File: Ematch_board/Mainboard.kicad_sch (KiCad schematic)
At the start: 69 parts, among them J10 Conn_01x02_Male, J11 Conn_Coaxial, J7 RBUS, J8 USB_C_Receptacle_USB2.0, J9 Conn_01x02_Male, Q1 MMDT2222A, U2 LTC4411, U3 SC4216H, U4 LTC4411, U5 SN65HVD230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

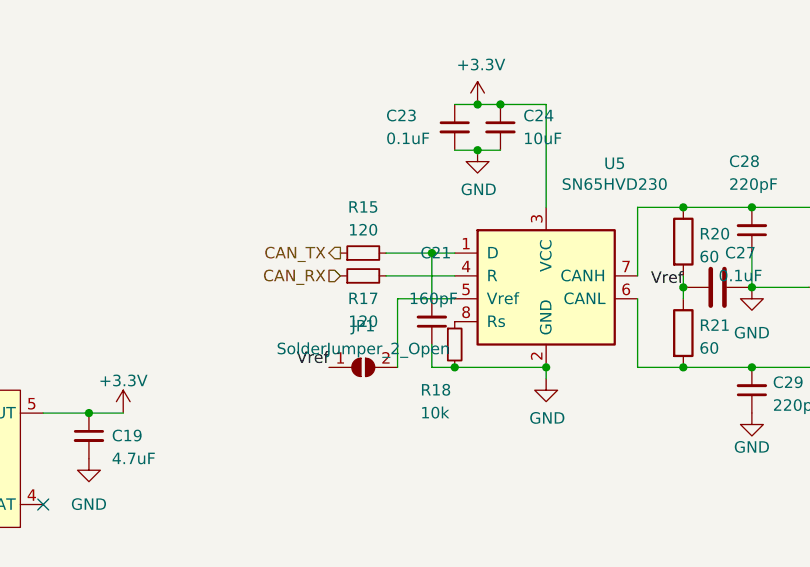
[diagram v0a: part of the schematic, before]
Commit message: Removed CAN resistors
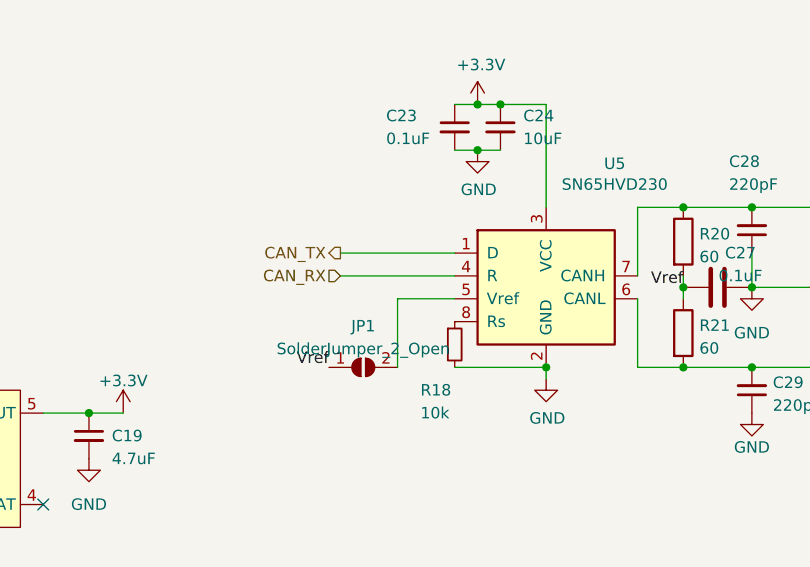
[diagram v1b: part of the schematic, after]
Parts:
- removed C21: 160pF, Capacitor_SMD:C_0603_1608Metric, symbol Device:C_Small
- removed R15, R17: 120, Resistor_SMD:R_0603_1608Metric, symbol Device:R_Small
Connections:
- net CAN_RX: now also U5.4 (R)
- net CAN_TX: now also U5.1 (D)
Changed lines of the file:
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@@
 (kicad_sch (version 20211123) (generator eeschema)
   (paper "A4")
-  (junction (at 190.5 162.56) (diameter 0) (color 0 0 0 0)
-  )
   (junction (at 219.71 53.34) (diameter 0) (color 0 0 0 0)
   )
@@
   (junction (at 203.2 106.68) (diameter 0) (color 0 0 0 0)
   )
-  (junction (at 187.96 149.86) (diameter 0) (color 0 0 0 0)
-  )
   (junction (at 199.39 38.1) (diameter 0) (color 0 0 0 0)
   )
@@
     (stroke (width 0) (type default) (color 0 0 0 0))
   )
-  (wire (pts (xy 187.96 160.02) (xy 187.96 162.56))
-    (stroke (width 0) (type default) (color 0 0 0 0))
-  )
   (wire (pts (xy 149.86 167.64) (xy 153.67 167.64))
     (stroke (width 0) (type default) (color 0 0 0 0))
@@
     (stroke (width 0) (type default) (color 0 0 0 0))
   )
-  (wire (pts (xy 182.88 152.4) (xy 190.5 152.4))
+  (wire (pts (xy 177.8 152.4) (xy 190.5 152.4))
     (stroke (width 0) (type default) (color 0 0 0 0))
   )
@@
     (stroke (width 0) (type default) (color 0 0 0 0))
   )
-  (wire (pts (xy 187.96 154.94) (xy 187.96 149.86))
-    (stroke (width 0) (type default) (color 0 0 0 0))
-  )
   (wire (pts (xy 124.46 93.98) (xy 132.08 93.98))
     (stroke (width 0) (type default) (color 0 0 0 0))
@@
     (stroke (width 0) (type default) (color 0 0 0 0))
   )
-  (wire (pts (xy 187.96 149.86) (xy 190.5 149.86))
+  (wire (pts (xy 177.8 149.86) (xy 190.5 149.86))
     (stroke (width 0) (type default) (color 0 0 0 0))
   )
@@
     (stroke (width 0) (type default) (color 0 0 0 0))
   )
-  (wire (pts (xy 187.96 162.56) (xy 190.5 162.56))
-    (stroke (width 0) (type default) (color 0 0 0 0))
-  )
   (wire (pts (xy 95.25 176.53) (xy 106.68 176.53))
     (stroke (width 0) (type default) (color 0 0 0 0))
@@
     (stroke (width 0) (type default) (color 0 0 0 0))
   )
-  (wire (pts (xy 182.88 149.86) (xy 187.96 149.86))
-    (stroke (width 0) (type default) (color 0 0 0 0))
-  )
   (wire (pts (xy 223.52 162.56) (xy 233.68 162.56))
     (stroke (width 0) (type default) (color 0 0 0 0))
@@
     (pin "4")
   )
-  (symbol (lib_id "Device:C_Small") (at 187.96 157.48 180) (unit 1)
-    (in_bom yes) (on_board yes)
-    (property "Reference" "C21" (id 0) (at 186.69 149.86 0)
-      (effects (font (size 1.27 1.27)) (justify right))
-    )
-    (property "Value" "160pF" (id 1) (at 185.42 154.94 0)
-      (effects (font (size 1.27 1.27)) (justify right))
-    )
-    (property "Footprint" "Capacitor_SMD:C_0603_1608Metric" (id 2) (at 187.96 157.48 0)
-      (effects (font (size 1.27 1.27)) hide)
-    )
-    (property "Datasheet" "~" (id 3) (at 187.96 157.48 0)
-      (effects (font (size 1.27 1.27)) hide)
-    )
-    (pin "1")
-    (pin "2")
-  )
   (symbol (lib_id "Device:C_Small") (at -15.24 33.02 270) (unit 1)
     (in_bom yes) (on_board yes)
@@
     (pin "2")
   )
-  (symbol (lib_id "Device:R_Small") (at 180.34 149.86 90) (unit 1)
-    (in_bom yes) (on_board yes)
-    (property "Reference" "R15" (id 0) (at 180.34 144.78 90))
-    (property "Value" "120" (id 1) (at 180.34 147.32 90))
-    (property "Footprint" "Resistor_SMD:R_0603_1608Metric" (id 2) (at 180.34 149.86 0)
-      (effects (font (size 1.27 1.27)) hide)
-    )
-    (property "Datasheet" "~" (id 3) (at 180.34 149.86 0)
-      (effects (font (size 1.27 1.27)) hide)
-    )
-    (pin "1")
-    (pin "2")
-  )
   (symbol (lib_id "iclr:RT9025-25GSP") (at 85.09 166.37 0) (unit 1)
     (in_bom yes) (on_board yes) (fields_autoplaced)
@@
     (pin "1")
   )
-  (symbol (lib_id "Device:R_Small") (at 180.34 152.4 90) (unit 1)
-    (in_bom yes) (on_board yes)
-    (property "Reference" "R17" (id 0) (at 180.34 154.94 90))
-    (property "Value" "120" (id 1) (at 180.34 157.48 90))
-    (property "Footprint" "Resistor_SMD:R_0603_1608Metric" (id 2) (at 180.34 152.4 0)
-      (effects (font (size 1.27 1.27)) hide)
-    )
-    (property "Datasheet" "~" (id 3) (at 180.34 152.4 0)
-      (effects (font (size 1.27 1.27)) hide)
-    )
-    (pin "1")
-    (pin "2")
-  )
   (symbol (lib_id "Device:C_Small") (at 149.86 170.18 0) (unit 1)
     (in_bom yes) (on_board yes)
@@
       (reference "C20") (unit 1) (value "4.7uF") (footprint "Capacitor_SMD:C_0603_1608Metric")
     )
-    (path "/71911f13-5bc4-475b-a824-f4b23da68d9e"
-      (reference "C21") (unit 1) (value "160pF") (footprint "Capacitor_SMD:C_0603_1608Metric")
-    )
     (path "/631c1919-897e-41c7-9678-4341d204cd53"
       (reference "C22") (unit 1) (value "1.0uF") (footprint "Capacitor_SMD:C_0603_1608Metric")
@@
       (reference "R14") (unit 1) (value "10K") (footprint "Resistor_SMD:R_0603_1608Metric")
     )
-    (path "/771ca9cf-590e-4238-82e8-b520d1b04fd1"
-      (reference "R15") (unit 1) (value "120") (footprint "Resistor_SMD:R_0603_1608Metric")
-    )
     (path "/00000000-0000-0000-0000-00005dab6448"
       (reference "R16") (unit 1) (value "470") (footprint "Resistor_SMD:R_0603_1608Metric")
     )
-    (path "/e9cdfc35-200a-4f5d-9419-dbce8b3696c7"
-      (reference "R17") (unit 1) (value "120") (footprint "Resistor_SMD:R_0603_1608Metric")
-    )
     (path "/ca919506-9328-4665-9351-074990933889"

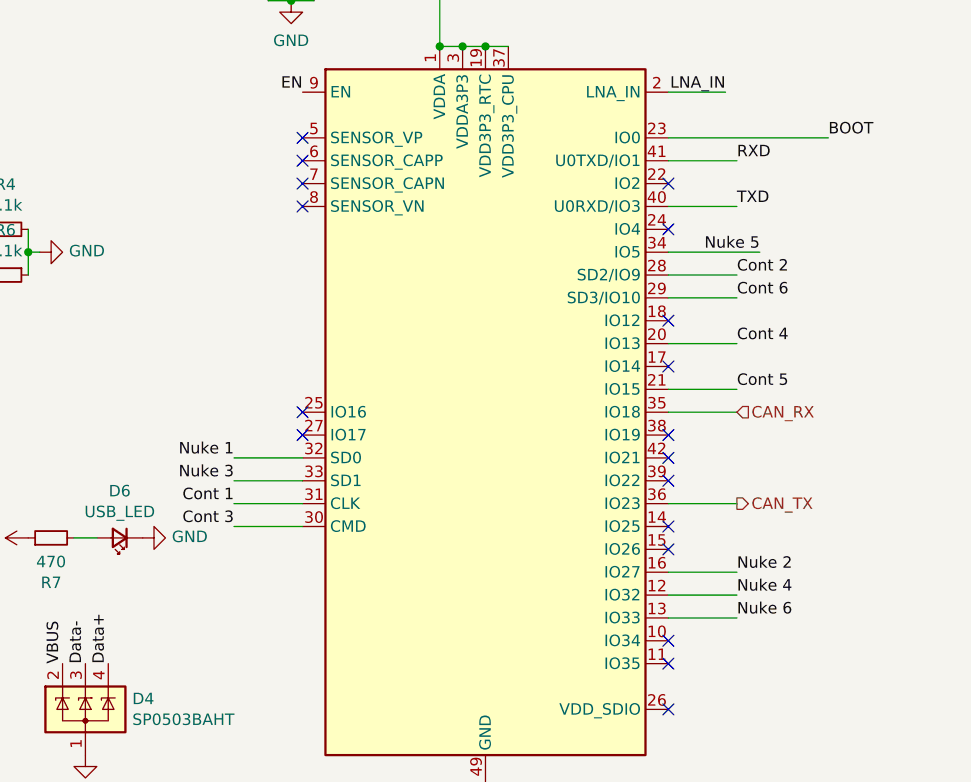
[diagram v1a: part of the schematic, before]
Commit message: Changed ESP32 pin assignment from special IO pins
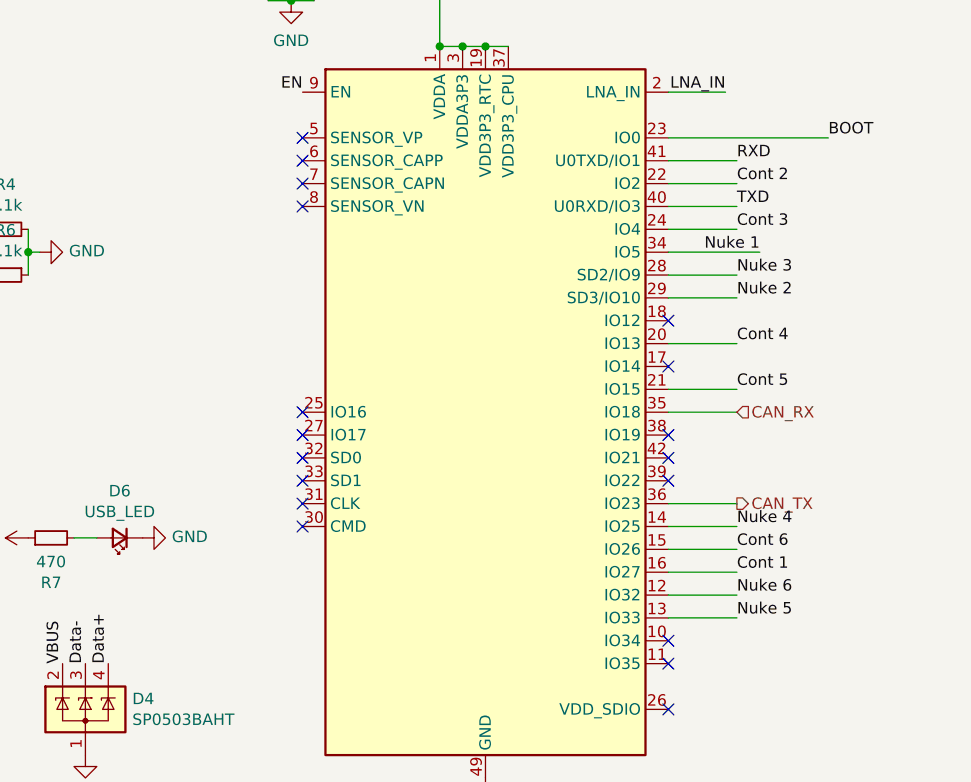
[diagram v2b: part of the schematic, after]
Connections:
- net Cont 1: now also GND1.16 (IO27); no longer GND1.31 (CLK)
- net Cont 2: now also GND1.22 (IO2); no longer GND1.28 (SD2/IO9)
- net Cont 3: now also GND1.24 (IO4); no longer GND1.30 (CMD)
- net Cont 6: now also GND1.15 (IO26); no longer GND1.29 (SD3/IO10)
- net Nuke 1: now also GND1.34 (IO5); no longer GND1.32 (SD0)
- net Nuke 2: now also GND1.29 (SD3/IO10); no longer GND1.16 (IO27)
- net Nuke 3: now also GND1.28 (SD2/IO9); no longer GND1.33 (SD1)
- net Nuke 4: now also GND1.14 (IO25); no longer GND1.12 (IO32)
- net Nuke 5: now also GND1.13 (IO33); no longer GND1.34 (IO5)
- net Nuke 6: now also GND1.12 (IO32); no longer GND1.13 (IO33)

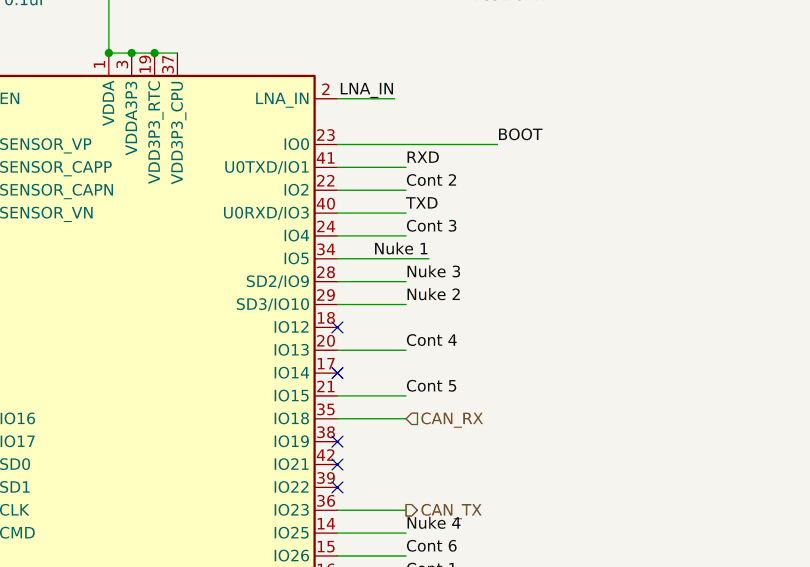
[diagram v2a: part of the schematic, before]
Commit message: Fixed pin assigments again
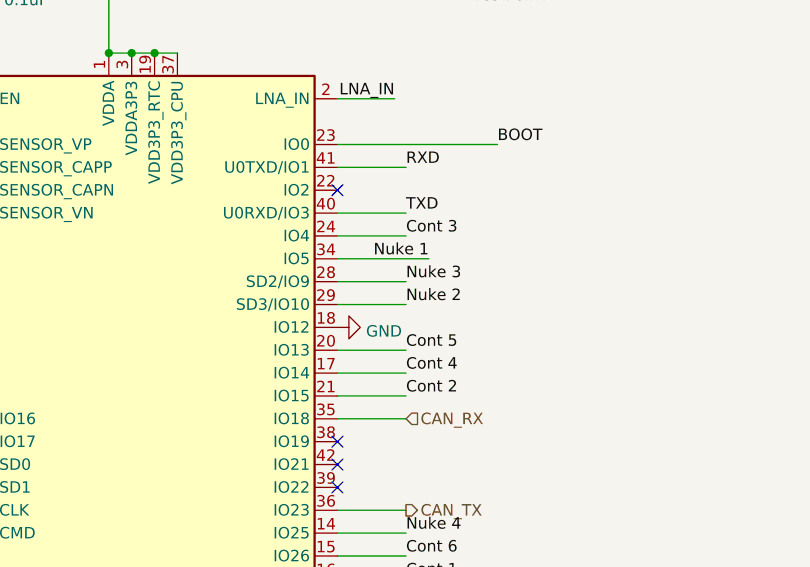
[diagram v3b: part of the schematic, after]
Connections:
- net Cont 2: now also GND1.21 (IO15); no longer GND1.22 (IO2)
- net Cont 4: now also GND1.17 (IO14); no longer GND1.20 (IO13)
- net Cont 5: now also GND1.20 (IO13); no longer GND1.21 (IO15)
- net GND: now also GND1.18 (IO12)
- no-connect marks 41 -> 40
